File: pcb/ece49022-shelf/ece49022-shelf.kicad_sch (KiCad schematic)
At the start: 0 parts

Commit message: quicksave
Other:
- sheet RP2350A ports: added GPIO0, GPIO1, GPIO10, GPIO2, GPIO3, GPIO4, GPIO5, GPIO6, GPIO7, GPIO8, GPIO9, I2C0_SCL, I2C0_SDA, I2C1_SCL, I2C1_SDA; removed none
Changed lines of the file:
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@@
 	(wire
 		(pts
-			(xy 52.07 97.79) (xy 59.69 97.79)
+			(xy 52.07 96.52) (xy 59.69 96.52)
 		)
 		(stroke
@@
 	(wire
 		(pts
-			(xy 59.69 95.25) (xy 59.69 97.79)
+			(xy 59.69 96.52) (xy 59.69 95.25)
 		)
 		(stroke
@@
 	(wire
 		(pts
-			(xy 59.69 83.82) (xy 59.69 86.36)
+			(xy 59.69 86.36) (xy 59.69 87.63)
 		)
 		(stroke
@@
 	(wire
 		(pts
-			(xy 52.07 86.36) (xy 59.69 86.36)
+			(xy 52.07 87.63) (xy 59.69 87.63)
 		)
 		(stroke
@@
 	(wire
 		(pts
-			(xy 25.4 83.82) (xy 25.4 86.36)
+			(xy 25.4 85.09) (xy 25.4 87.63)
 		)
 		(stroke
@@
 	(wire
 		(pts
-			(xy 33.02 86.36) (xy 25.4 86.36)
+			(xy 33.02 87.63) (xy 25.4 87.63)
 		)
 		(stroke
@@
 	(symbol
 		(lib_id "power:+3V3")
-		(at 59.69 83.82 0)
+		(at 59.69 86.36 0)
 		(unit 1)
 		(exclude_from_sim no)
@@
 		(fields_autoplaced yes)
 		(property "Reference" "#PWR012"
-			(at 59.69 87.63 0)
+			(at 59.69 90.17 0)
 			(effects
 				(font
@@
 		)
 		(property "Value" "+3V3"
-			(at 59.69 78.74 0)
+			(at 59.69 81.28 0)
 			(effects
 				(font
@@
 		)
 		(property "Footprint" ""
-			(at 59.69 83.82 0)
+			(at 59.69 86.36 0)
 			(effects
 				(font
@@
 		)
 		(property "Datasheet" ""
-			(at 59.69 83.82 0)
+			(at 59.69 86.36 0)
 			(effects
 				(font
@@
 		)
 		(property "Description" "Power symbol creates a global label with name \"+3V3\""
-			(at 59.69 83.82 0)
+			(at 59.69 86.36 0)
 			(effects
 				(font
@@
 	(symbol
 		(lib_id "power:+12V")
-		(at 25.4 83.82 0)
+		(at 25.4 85.09 0)
 		(unit 1)
 		(exclude_from_sim no)
@@
 		(fields_autoplaced yes)
 		(property "Reference" "#PWR011"
-			(at 25.4 87.63 0)
+			(at 25.4 88.9 0)
 			(effects
 				(font
@@
 		)
 		(property "Value" "+12V"
-			(at 25.4 78.74 0)
+			(at 25.4 80.01 0)
 			(effects
 				(font
@@
 		)
 		(property "Footprint" ""
-			(at 25.4 83.82 0)
+			(at 25.4 85.09 0)
 			(effects
 				(font
@@
 		)
 		(property "Datasheet" ""
-			(at 25.4 83.82 0)
+			(at 25.4 85.09 0)
 			(effects
 				(font
@@
 		)
 		(property "Description" "Power symbol creates a global label with name \"+12V\""
-			(at 25.4 83.82 0)
+			(at 25.4 85.09 0)
 			(effects
 				(font
@@
 		)
 		(pin "5V" input
-			(at 52.07 97.79 0)
+			(at 52.07 96.52 0)
 			(effects
 				(font
@@
 		)
 		(pin "3.3V" input
-			(at 52.07 86.36 0)
+			(at 52.07 87.63 0)
 			(effects
 				(font
@@
 		)
 		(pin "12V" input
-			(at 33.02 86.36 180)
+			(at 33.02 87.63 180)
 			(effects
 				(font
@@
 			)
 		)
+		(pin "GPIO7" input
+			(at 135.89 97.79 0)
+			(effects
+				(font
+					(size 1.27 1.27)
+				)
+				(justify right)
+			)
+		)
+		(pin "I2C1_SDA" input
+			(at 95.25 80.01 180)
+			(effects
+				(font
+					(size 1.27 1.27)
+				)
+				(justify left)
+			)
+		)
+		(pin "GPIO2" input
+			(at 135.89 85.09 0)
+			(effects
+				(font
+					(size 1.27 1.27)
+				)
+				(justify right)
+			)
+		)
+		(pin "GPIO8" input
+			(at 135.89 100.33 0)
+			(effects
+				(font
+					(size 1.27 1.27)
+				)
+				(justify right)
+			)
+		)
+		(pin "GPIO3" input
+			(at 135.89 87.63 0)
+			(effects
+				(font
+					(size 1.27 1.27)
+				)
+				(justify right)
+			)
+		)
+		(pin "GPIO0" input
+			(at 135.89 80.01 0)
+			(effects
+				(font
+					(size 1.27 1.27)
+				)
+				(justify right)
+			)
+		)
+		(pin "GPIO1" input
+			(at 135.89 82.55 0)
+			(effects
+				(font
+					(size 1.27 1.27)
+				)
+				(justify right)
+			)
+		)
+		(pin "GPIO5" input
+			(at 135.89 92.71 0)
+			(effects
+				(font
+					(size 1.27 1.27)
+				)
+				(justify right)
+			)
+		)
+		(pin "GPIO9" input
+			(at 135.89 102.87 0)
+			(effects
+				(font
+					(size 1.27 1.27)
+				)
+				(justify right)
+			)
+		)
+		(pin "I2C1_SCL" input
+			(at 95.25 82.55 180)
+			(effects
+				(font
+					(size 1.27 1.27)
+				)
+				(justify left)
+			)
+		)
+		(pin "GPIO4" input
+			(at 135.89 90.17 0)
+			(effects
+				(font
+					(size 1.27 1.27)
+				)
+				(justify right)
+			)
+		)
+		(pin "GPIO10" input
+			(at 135.89 105.41 0)
+			(effects
+				(font
+					(size 1.27 1.27)
+				)
+				(justify right)
+			)
+		)
+		(pin "GPIO6" input
+			(at 135.89 95.25 0)
+			(effects
+				(font
+					(size 1.27 1.27)
+				)
+				(justify right)
+			)
+		)
+		(pin "I2C0_SDA" input
+			(at 95.25 87.63 180)
+			(effects
+				(font
+					(size 1.27 1.27)
+				)
+				(justify left)
+			)
+		)
+		(pin "I2C0_SCL" input
+			(at 95.25 90.17 180)
+			(effects
+				(font
+					(size 1.27 1.27)
+				)
+				(justify left)
+			)
+		)
 		(instances
 			(project "ece49022-shelf"
@@
 	)
 	(sheet
-		(at 182.88 72.39)
+		(at 29.21 26.67)
 		(size 29.21 40.64)
 		(exclude_from_sim no)
@@
 		)
 		(property "Sheetname" "NAU7802"
-			(at 182.88 71.6784 0)
+			(at 29.21 25.9584 0)
 			(effects
 				(font
@@
 		)
 		(property "Sheetfile" "NAU7802.kicad_sch"
-			(at 182.88 113.6146 0)
+			(at 29.21 67.8946 0)
 			(effects
 				(font
@@
 		)
 		(pin "E-" input
-			(at 212.09 105.41 0)
+			(at 58.42 59.69 0)
 			(effects
 				(font
@@
 		)
 		(pin "E+" input
-			(at 212.09 99.06 0)
+			(at 58.42 53.34 0)
 			(effects
 				(font
@@
 		)
 		(pin "Green" input
-			(at 212.09 91.44 0)
+			(at 58.42 45.72 0)
 			(effects
 				(font
@@
 		)
 		(pin "White" input
-			(at 212.09 82.55 0)
+			(at 58.42 36.83 0)
 			(effects
 				(font
@@
 		)
 		(pin "DRDY" input
-			(at 182.88 82.55 180)
+			(at 29.21 36.83 180)
 			(effects
 				(font
@@
 		)
 		(pin "SCLK" input
-			(at 182.88 90.17 180)
+			(at 29.21 44.45 180)
 			(effects
 				(font
@@
 		)
 		(pin "SDIO" input
-			(at 182.88 100.33 180)
-			(effects
-				(font
+			(at 29.21 54.61 180)
+			(effects
+				(font

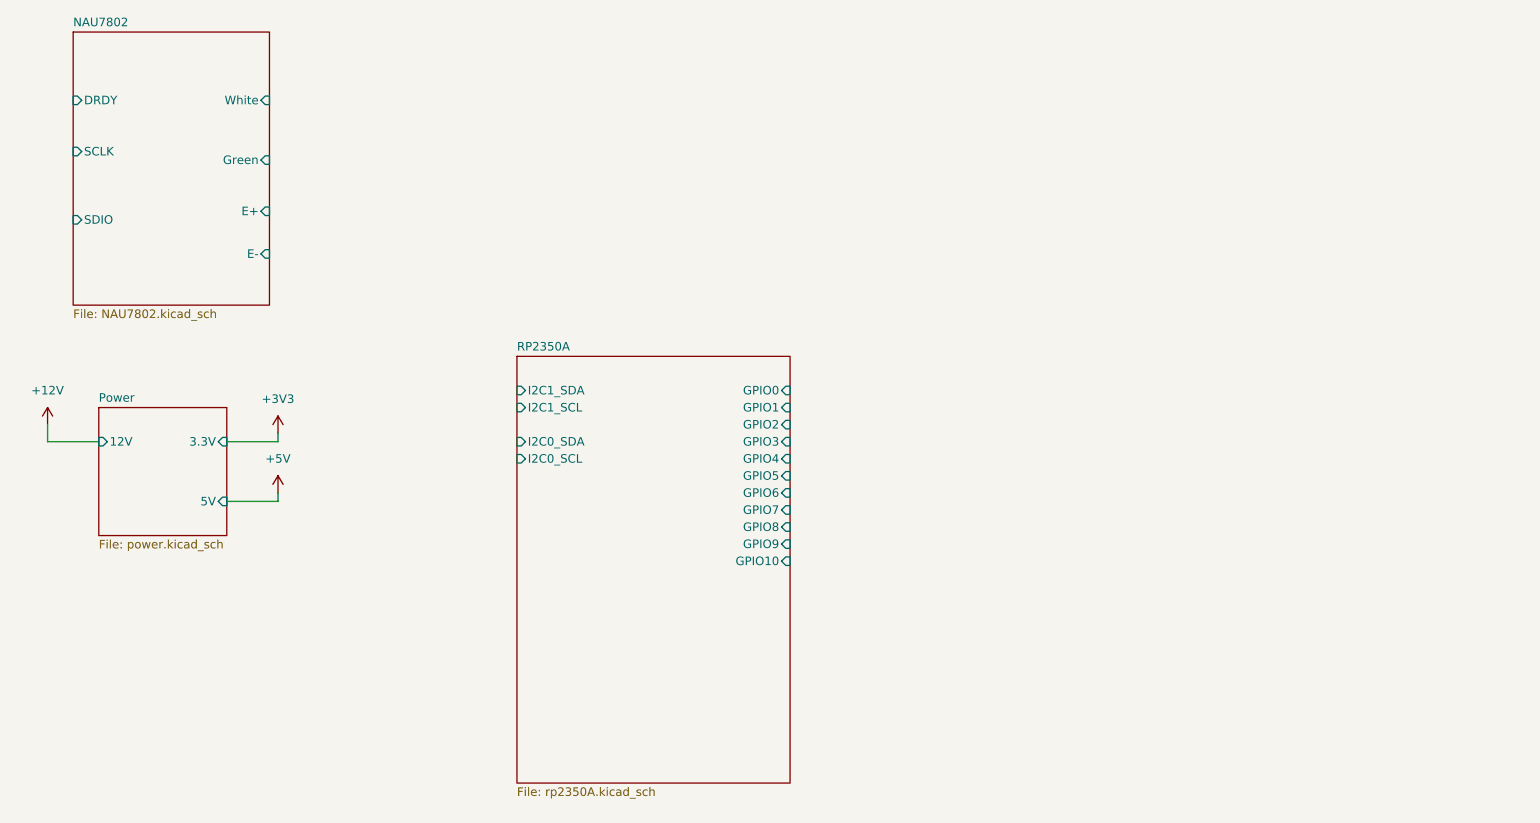
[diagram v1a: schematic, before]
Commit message: connecting top level
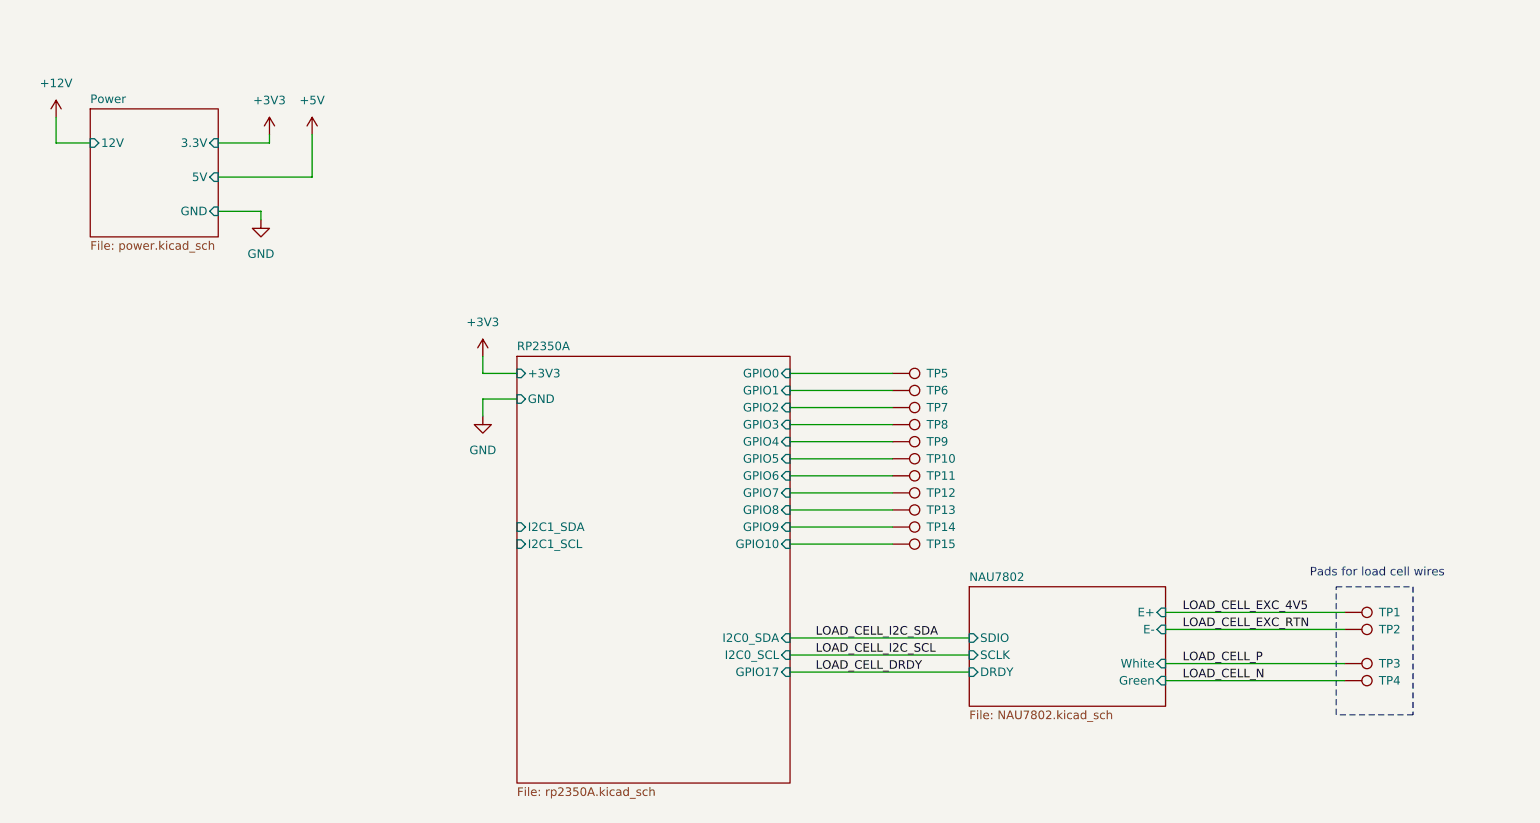
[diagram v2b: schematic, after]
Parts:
- added TP1, TP10, TP11, TP12, TP13, TP14, TP15, TP2, TP3, TP4, TP5, TP6, TP7, TP8, TP9: TestPoint, symbol Connector:TestPoint
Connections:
- net RP2350A/GPIO0: now also TP5.1
- net RP2350A/GPIO1: now also TP6.1
- net RP2350A/GPIO10: now also TP15.1
- net RP2350A/GPIO2: now also TP7.1
- net RP2350A/GPIO3: now also TP8.1
- net RP2350A/GPIO4: now also TP9.1
- net RP2350A/GPIO5: now also TP10.1
- net RP2350A/GPIO6: now also TP11.1
- net RP2350A/GPIO7: now also TP12.1
- net RP2350A/GPIO8: now also TP13.1
- net RP2350A/GPIO9: now also TP14.1
- new net LOAD_CELL_EXC_4V5: TP1.1
- new net LOAD_CELL_EXC_RTN: TP2.1
- new net LOAD_CELL_N: TP4.1
- new net LOAD_CELL_P: TP3.1
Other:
- sheet Power ports: added GND; removed none
- sheet RP2350A ports: added +3V3, GND, GPIO17; removed none
- note added: "Pads for load cell wires"

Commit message: added power
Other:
- sheet NAU7802 ports: added +5V; removed none
- moved on the sheet: TP10, TP11, TP12, TP13, TP14, TP15, TP5, TP6, TP7, TP8, TP9

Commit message: test
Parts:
- removed TP10, TP11, TP12, TP13, TP14, TP15, TP5, TP6, TP7, TP8, TP9: TestPoint, symbol Connector:TestPoint
- added J2: Conn_01x16_Pin, symbol Connector:Conn_01x16_Pin
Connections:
- net RP2350A/GPIO0: now also J2.4 (Pin_4)
- net RP2350A/GPIO1: now also J2.5 (Pin_5)
- net RP2350A/GPIO10: now also J2.14 (Pin_14)
- net RP2350A/GPIO2: now also J2.6 (Pin_6)
- net RP2350A/GPIO3: now also J2.7 (Pin_7)
- net RP2350A/GPIO4: now also J2.8 (Pin_8)
- net RP2350A/GPIO5: now also J2.9 (Pin_9)
- net RP2350A/GPIO6: now also J2.10 (Pin_10)
- net RP2350A/GPIO7: now also J2.11 (Pin_11)
- net RP2350A/GPIO8: now also J2.12 (Pin_12)
- net RP2350A/GPIO9: now also J2.13 (Pin_13)
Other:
- moved on the sheet: TP1, TP2, TP3, TP4

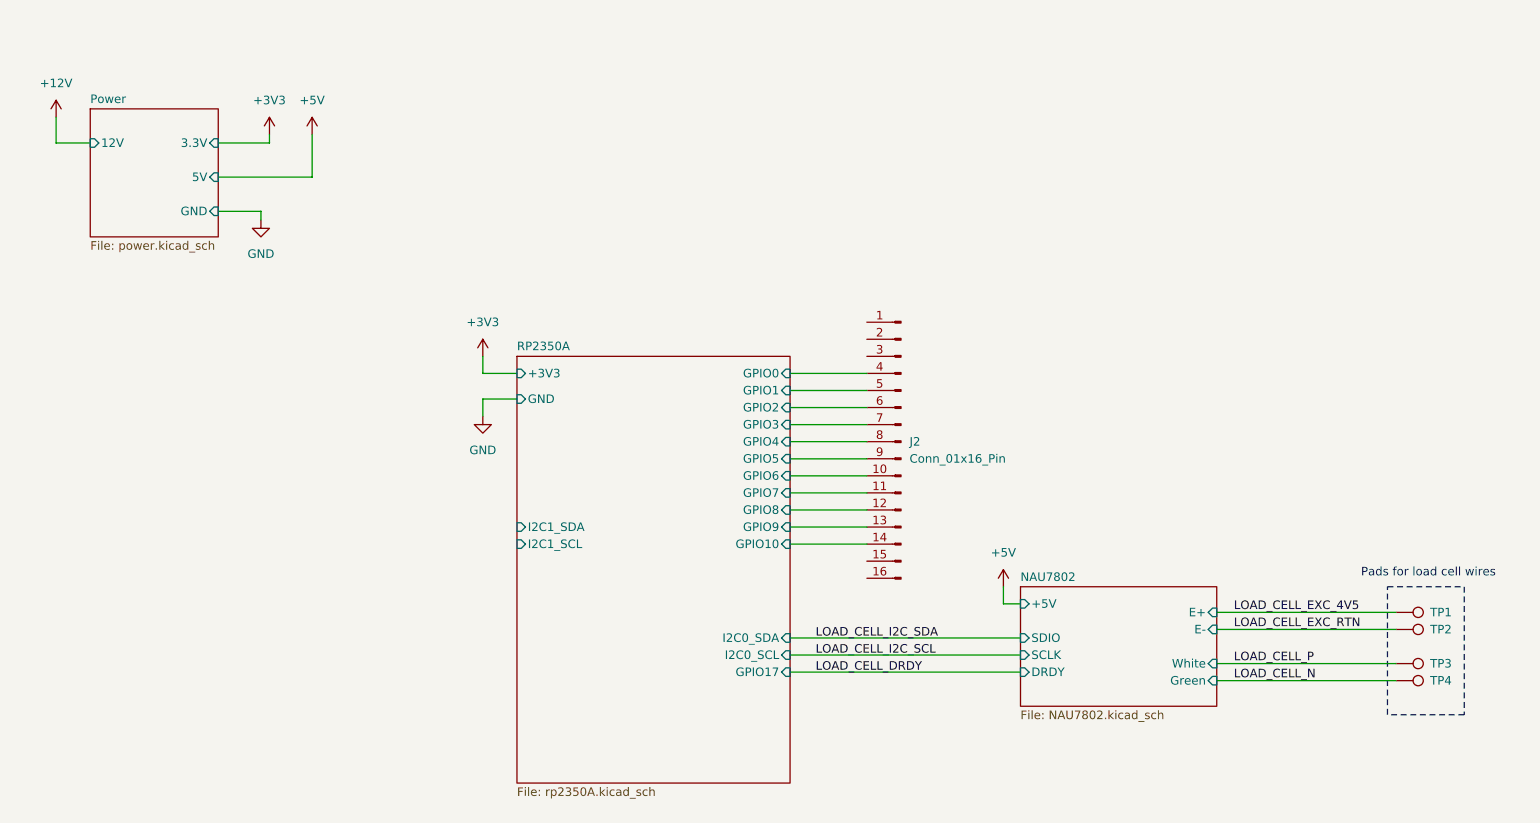
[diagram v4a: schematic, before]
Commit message: Added LCD Pins
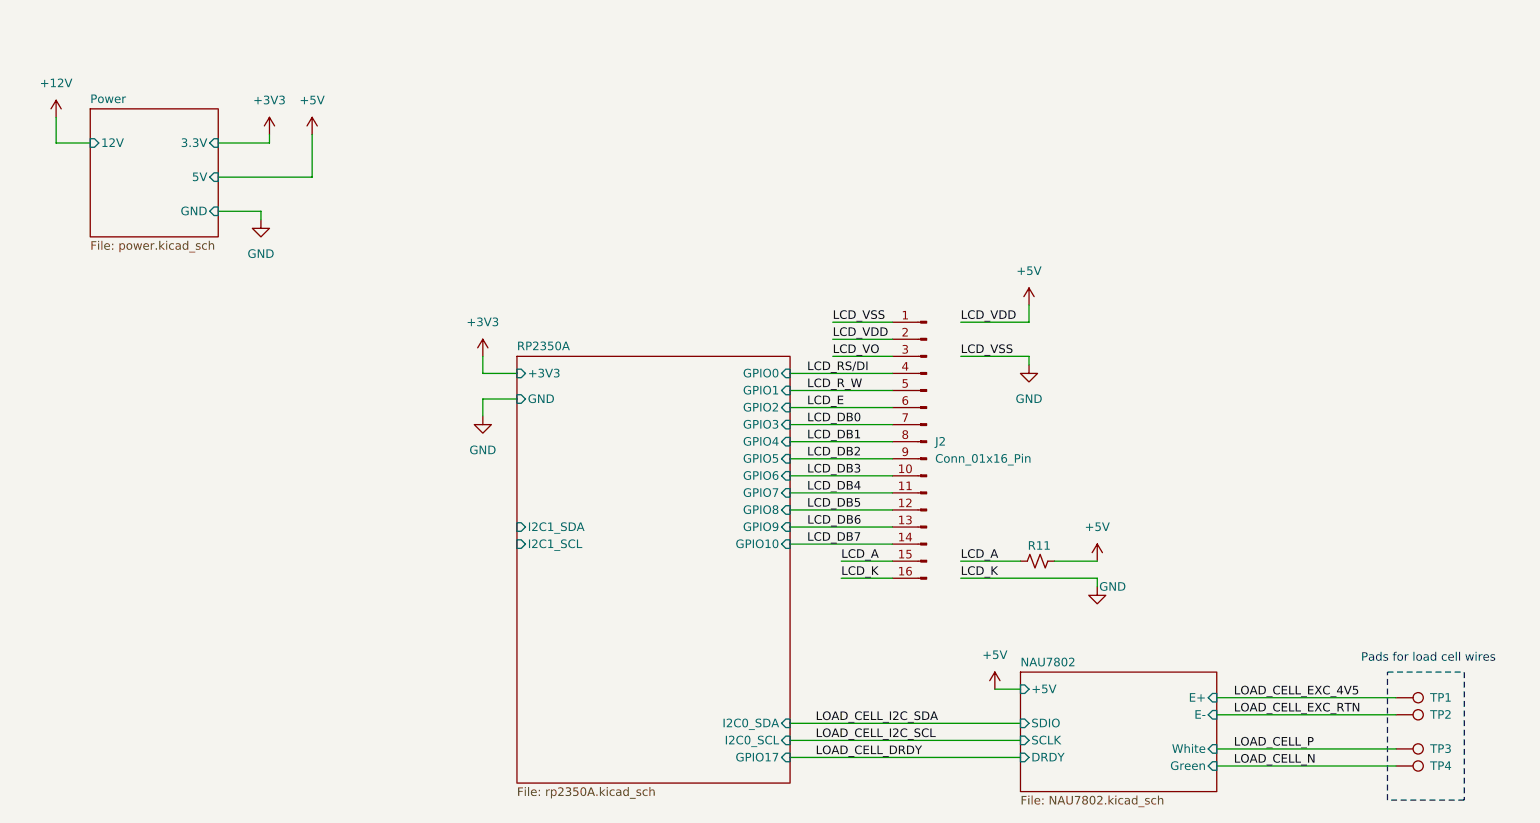
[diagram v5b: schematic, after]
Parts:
- added R11: R_Small_US, symbol Device:R_Small_US
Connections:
- net +5V: now also J2.2 (Pin_2), R11.2
- net GND: now also J2.1 (Pin_1), J2.16 (Pin_16)
- net LCD_A: now reaches J2.15 (Pin_15)
- net LCD_A: now also R11.1
- net LCD_VO: now reaches J2.3 (Pin_3)
- net RP2350A/GPIO0 renamed LCD_RS/DI
- net RP2350A/GPIO1 renamed LCD_R_W
- net RP2350A/GPIO10 renamed LCD_DB7
- net RP2350A/GPIO2 renamed LCD_E
- net RP2350A/GPIO3 renamed LCD_DB0
- net RP2350A/GPIO4 renamed LCD_DB1
- net RP2350A/GPIO5 renamed LCD_DB2
- net RP2350A/GPIO6 renamed LCD_DB3
- net RP2350A/GPIO7 renamed LCD_DB4
- net RP2350A/GPIO8 renamed LCD_DB5
- net RP2350A/GPIO9 renamed LCD_DB6
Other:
- moved on the sheet: J2, TP1, TP2, TP3, TP4

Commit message: added LCD and offboard connectors
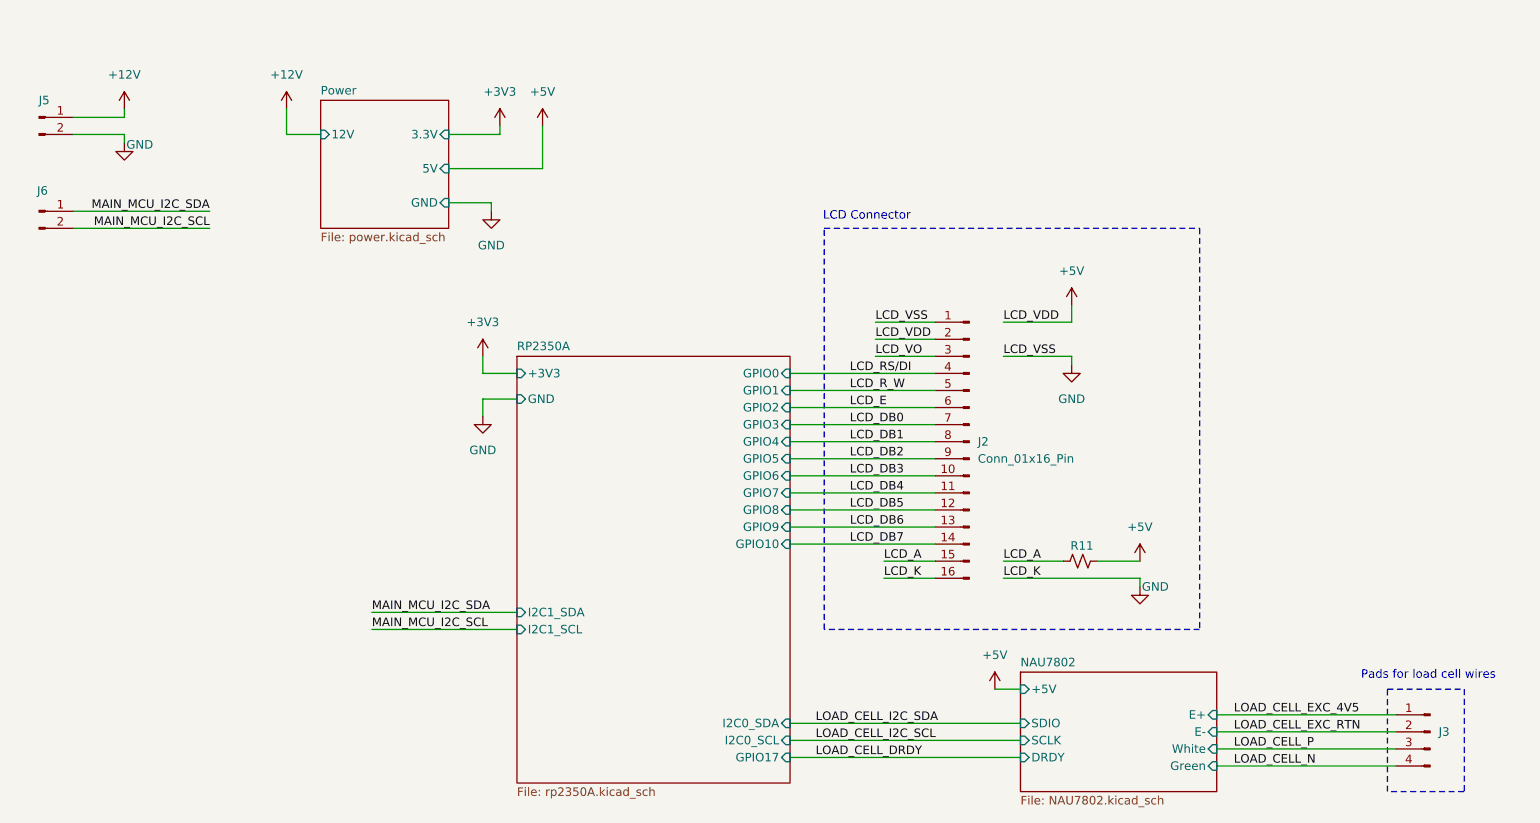
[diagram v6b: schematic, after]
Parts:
- removed TP1, TP2, TP3, TP4: TestPoint, symbol Connector:TestPoint
- added J3: Conn_01x04_Pin, symbol Connector:Conn_01x04_Pin
- added J5, J6: Conn_01x02_Pin, symbol Connector:Conn_01x02_Pin
- J2: footprint (none) -> Connector_PinSocket_2.54mm:PinSocket_1x16_P2.54mm_Vertical
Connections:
- net +12V: now also J5.1 (Pin_1)
- net GND: now also J5.2 (Pin_2)
- net LOAD_CELL_EXC_4V5: now also J3.1 (Pin_1)
- net LOAD_CELL_EXC_RTN: now also J3.2 (Pin_2)
- net LOAD_CELL_N: now also J3.4 (Pin_4)
- net LOAD_CELL_P: now also J3.3 (Pin_3)
- new net MAIN_MCU_I2C_SCL: J6.2 (Pin_2)
- new net MAIN_MCU_I2C_SDA: J6.1 (Pin_1)
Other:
- note added: "LCD Connector"
- moved on the sheet: J2, R11

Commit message: forgot to push some stuff
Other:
- note added: "Off Board Power + Comms"
- moved on the sheet: J5, J6
